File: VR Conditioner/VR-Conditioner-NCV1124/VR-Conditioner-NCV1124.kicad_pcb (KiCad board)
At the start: 2 copper layers, 18.7 x 17.9 mm, 9 parts, among them J1 NCV1124DR2G, J2 Board Conn

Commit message: Add prod files for NVC1124
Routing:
- added copper zone on B.Cu, net GND
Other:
- board text added: "Designed by Henrik Heininen HEINISET.FI (c) 2026"
- board text removed: "Designed by HEINISET.FI (c) 2026"
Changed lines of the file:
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@@
 			(usegerberattributes yes)
 			(usegerberadvancedattributes yes)
-			(creategerberjobfile yes)
+			(creategerberjobfile no)
 			(dashed_line_dash_ratio 12.000000)
 			(dashed_line_gap_ratio 3.000000)
@@
 			(outputformat 1)
 			(mirror no)
-			(drillshape 1)
+			(drillshape 0)
 			(scaleselection 1)
-			(outputdirectory "")
+			(outputdirectory "./gerbers")
 		)
 	)
@@
 			)
 		)
+		(property "LCSC" "C17414"
+			(at 0 0 0)
+			(layer "F.SilkS")
+			(hide yes)
+			(effects
+				(font
+					(size 1.27 1.27)
+					(thickness 0.15)
+				)
+			)
+		)
 		(property ki_fp_filters "R_*")
 		(sheetname "/")
@@
 			)
 		)
+		(property "LCSC" "C49678"
+			(at 0 0 0)
+			(layer "F.SilkS")
+			(hide yes)
+			(effects
+				(font
+					(size 1.27 1.27)
+					(thickness 0.15)
+				)
+			)
+		)
 		(property ki_fp_filters "C_*")
 		(sheetname "/")
@@
 			(at 0 0 90)
 			(layer "F.Fab")
+			(hide yes)
+			(effects
+				(font
+					(size 1.27 1.27)
+					(thickness 0.15)
+				)
+			)
+		)
+		(property "LCSC" "C17414"
+			(at 0 0 0)
+			(layer "F.SilkS")
 			(hide yes)
 			(effects
@@
 			)
 		)
+		(property "LCSC" "C49678"
+			(at 0 0 0)
+			(layer "F.SilkS")
+			(hide yes)
+			(effects
+				(font
+					(size 1.27 1.27)
+					(thickness 0.15)
+				)
+			)
+		)
 		(property ki_fp_filters "C_*")
 		(sheetname "/")
@@
 			)
 		)
+		(property "LCSC" "C49678"
+			(at 0 0 0)
+			(layer "F.SilkS")
+			(hide yes)
+			(effects
+				(font
+					(size 1.27 1.27)
+					(thickness 0.15)
+				)
+			)
+		)
 		(property ki_fp_filters "C_*")
 		(sheetname "/")
@@
 		(sheetname "/")
 		(sheetfile "VR-Conditioner-NCV1124.kicad_sch")
-		(attr smd)
+		(attr smd exclude_from_pos_files exclude_from_bom)
 		(fp_line
 			(start -0.261252 0.735)
@@
 				(font
 					(size 1 1)
+					(thickness 0.15)
+				)
+			)
+		)
+		(property "LCSC" "C152274"
+			(at 0 0 0)
+			(layer "F.SilkS")
+			(hide yes)
+			(effects
+				(font
+					(size 1.27 1.27)
 					(thickness 0.15)
 				)
@@
 		(layer "Edge.Cuts")
 	)
-	(gr_text "Designed by HEINISET.FI\n(c) 2026"
-		(at 155.194 77.216 0)
+	(gr_text "Designed by Henrik Heininen\nHEINISET.FI\n(c) 2026"
+		(at 155.2448 78.5368 0)
 		(layer "B.SilkS")
 		(effects
@@
 		(net 10)
 		(net_name "GND")
-		(layer "F.Cu")
+		(layers "F.Cu" "B.Cu")
 		(hatch edge 0.5)
 		(connect_pads yes

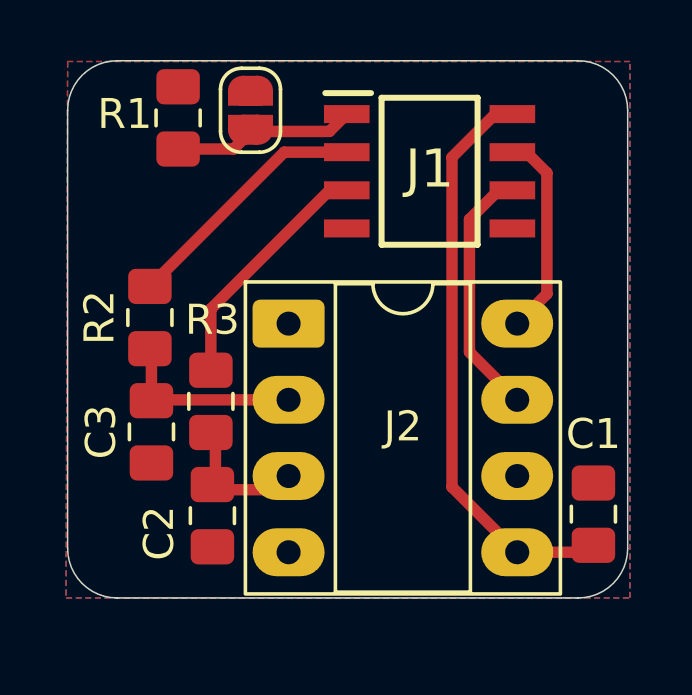
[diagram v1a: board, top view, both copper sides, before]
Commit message: Changed to THT resistors due to wattage requirements as per ncv1124 datasheet. Added prod files
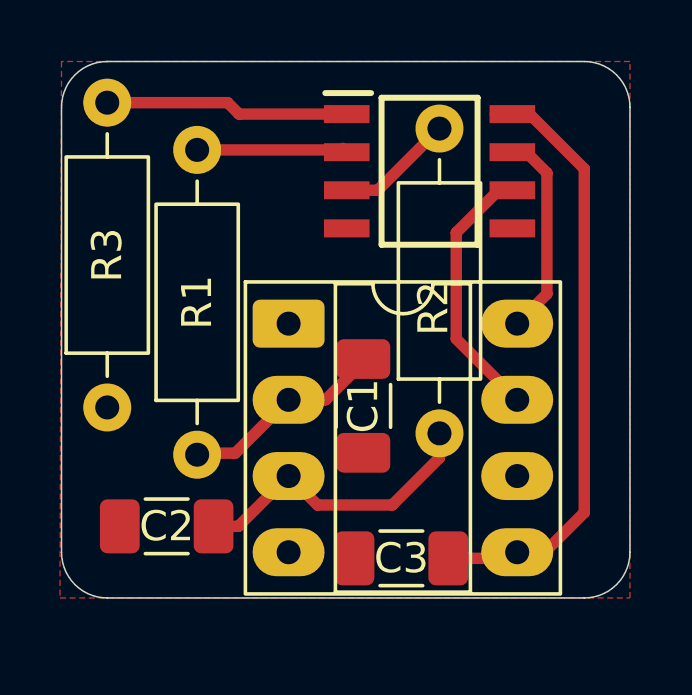
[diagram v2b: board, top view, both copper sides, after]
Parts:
- removed JP1: SolderJumper_2_Open, Jumper:SolderJumper-2_P1.3mm_Open_RoundedPad1.0x1.5mm
- C1: renamed from C3; value 100n -> 1nF; footprint Capacitor_SMD:C_0805_2012Metric_Pad1.18x1.45mm_HandSolder -> Capacitor_SMD:C_1206_3216Metric_Pad1.33x1.80mm_HandSolder
- C2: value 100n -> 1nF; footprint Capacitor_SMD:C_0805_2012Metric_Pad1.18x1.45mm_HandSolder -> Capacitor_SMD:C_1206_3216Metric_Pad1.33x1.80mm_HandSolder
- C3: renamed from C1; footprint Capacitor_SMD:C_0805_2012Metric_Pad1.18x1.45mm_HandSolder -> Capacitor_SMD:C_1206_3216Metric_Pad1.33x1.80mm_HandSolder
- R1: renamed from R2; value 10k -> 15k; footprint Capacitor_SMD:C_0805_2012Metric_Pad1.18x1.45mm_HandSolder -> Resistor_THT:R_Axial_DIN0207_L6.3mm_D2.5mm_P10.16mm_Horizontal
- R2: renamed from R3; value 10k -> 15k; footprint Capacitor_SMD:C_0805_2012Metric_Pad1.18x1.45mm_HandSolder -> Resistor_THT:R_Axial_DIN0207_L6.3mm_D2.5mm_P10.16mm_Horizontal
- R3: renamed from R1; value Rtrip -> Rtrip / 17k8; footprint Capacitor_SMD:C_0805_2012Metric_Pad1.18x1.45mm_HandSolder -> Resistor_THT:R_Axial_DIN0207_L6.3mm_D2.5mm_P10.16mm_Horizontal
- moved R3 9.94 mm to (147.1, 86.6), turned to 90 degrees
- moved R2 7.69 mm to (158.2, 87.5)
- moved C1 7.11 mm to (155.7, 86.6)
- moved C3 6.57 mm to (156.9, 91.6), turned to 0 degrees
- moved R1 4.84 mm to (150.1, 88.2)
- moved C2 1.56 mm to (149.1, 90.6), turned to 180 degrees
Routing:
- net IN2+: track 4.60 -> 10.1 mm
- net Net-(J1-IN2): track 8.21 -> 4.52 mm
- net Net-(J1-IN1): track 8.42 -> 5.20 mm
- net Net-(J1-INADJ): track 6.10 -> 8.14 mm
- net IN1+: track 6.23 -> 7.43 mm
- net VCC: track 19.3 -> 20.4 mm
- removed copper zone on B.Cu, net GND
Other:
- board size 18.7 x 17.9 mm -> 18.9 x 17.9 mm

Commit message: Small brainfart with the layout. Updated pcb and gerbers
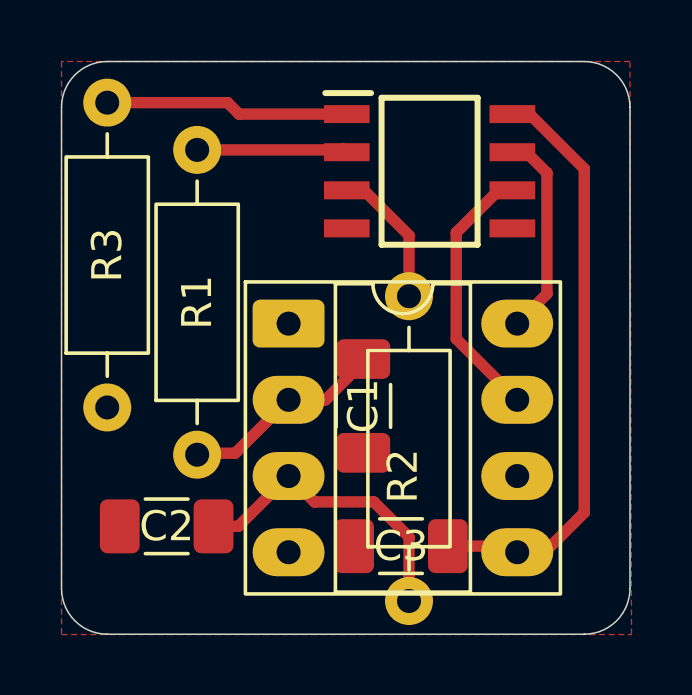
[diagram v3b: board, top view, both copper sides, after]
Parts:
- moved R2 5.68 mm to (157.2, 93.1)
- moved C3 0.41 mm to (156.9, 91.2)
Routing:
- net Net-(J1-IN2): track 4.52 -> 5.30 mm
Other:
- board size 18.9 x 17.9 mm -> 18.9 x 19.1 mm
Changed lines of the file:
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@@
 	(footprint "Capacitor_SMD:C_1206_3216Metric_Pad1.33x1.80mm_HandSolder"
 		(layer "F.Cu")
-		(at 156.9212 91.6432)
+		(at 156.9089 91.2368)
 		(descr "Capacitor SMD 1206 (3216 Metric), square (rectangular) end terminal, IPC-7351 nominal with elongated pad for handsoldering. (Body size source: IPC-SM-782 page 76, https://www.pcb-3d.com/wordpress/wp-content/uploads/ipc-sm-782a_amendment_1_and_2.pdf), generated with kicad-footprint-generator")
 		(tags "capacitor handsolder")
@@
 	(footprint "Resistor_THT:R_Axial_DIN0207_L6.3mm_D2.5mm_P10.16mm_Horizontal"
 		(layer "F.Cu")
-		(at 158.1912 87.4776 90)
+		(at 157.1752 93.0656 90)
 		(descr "Resistor, Axial_DIN0207 series, Axial, Horizontal, pin pitch=10.16mm, 0.25W = 1/4W, length*diameter=6.3*2.5mm^2, http://cdn-reichelt.de/documents/datenblatt/B400/1_4W%23YAG.pdf")
 		(tags "Resistor Axial_DIN0207 series Axial Horizontal pin pitch 10.16mm 0.25W = 1/4W length 6.3mm diameter 2.5mm")
@@
 	)
 	(gr_arc
-		(start 147.1168 92.964)
-		(mid 146.039169 92.517631)
-		(end 145.5928 91.44)
+		(start 147.1168 94.172369)
+		(mid 146.039169 93.726)
+		(end 145.5928 92.648369)
 		(stroke
 			(width 0.05)
@@
 	)
 	(gr_line
-		(start 164.5412 91.44)
+		(start 164.5412 92.6484)
 		(end 164.5412 76.6064)
 		(stroke
@@
 	)
 	(gr_arc
-		(start 164.5412 91.44)
-		(mid 164.094831 92.517631)
-		(end 163.0172 92.964)
+		(start 164.5412 92.648369)
+		(mid 164.094831 93.726)
+		(end 163.0172 94.172369)
 		(stroke
 			(width 0.05)
@@
 	(gr_line
 		(start 145.5928 76.6064)
-		(end 145.5928 91.44)
+		(end 145.5928 92.648369)
 		(stroke
 			(width 0.05)
@@
 	)
 	(gr_line
-		(start 147.1168 92.964)
-		(end 163.0172 92.964)
+		(start 147.1168 94.172369)
+		(end 163.0172 94.172369)
 		(stroke
 			(width 0.05)
@@
 	)
 	(segment
+		(start 158.4714 91.2368)
+		(end 160.5788 91.2368)
+		(width 0.381)
+		(layer "F.Cu")
+		(net 1)
+	)
+	(segment
 		(start 163.0172 90.1192)
 		(end 163.0172 78.6582)
@@
 	)
 	(segment
-		(start 158.4837 91.6432)
-		(end 160.5788 91.6432)
+		(start 160.5788 91.2368)
+		(end 160.782 91.44)
 		(width 0.381)
 		(layer "F.Cu")
@@
 	)
 	(segment
-		(start 154.1272 89.8652)
-		(end 153.162 88.9)
+		(start 157.1752 90.932)
+		(end 157.1752 93.0656)
+		(width 0.381)
+		(layer "F.Cu")
+		(net 2)
+	)
+	(segment
+		(start 156.0068 89.7636)
+		(end 157.1752 90.932)
+		(width 0.381)
+		(layer "F.Cu")
+		(net 2)
+	)
+	(segment
+		(start 154.0256 89.7636)
+		(end 156.0068 89.7636)
+		(width 0.381)
+		(layer "F.Cu")
+		(net 2)
+	)
+	(segment
+		(start 153.162 88.9)
+		(end 154.0256 89.7636)
 		(width 0.381)
 		(layer "F.Cu")
@@
 	)
 	(segment
-		(start 156.6164 89.8652)
-		(end 154.1272 89.8652)
-		(width 0.381)
-		(layer "F.Cu")
-		(net 2)
-	)
-	(segment
-		(start 158.1912 88.2904)
-		(end 156.6164 89.8652)
-		(width 0.381)
-		(layer "F.Cu")
-		(net 2)
-	)
-	(segment
 		(start 153.162 88.9)
 		(end 151.4856 90.5764)
@@
 	)
 	(segment
-		(start 158.1912 87.4776)
-		(end 158.1912 88.2904)
-		(width 0.381)
-		(layer "F.Cu")
-		(net 2)
-	)
-	(segment
 		(start 149.733 88.138)
 		(end 151.384 88.138)
@@
 	)
 	(segment
+		(start 155.101 79.375)
+		(end 155.674 79.375)
+		(width 0.381)
+		(layer "F.Cu")
+		(net 4)
+	)
+	(segment
 		(start 154.528 79.375)
 		(end 155.101 79.375)
@@
 	)
 	(segment
-		(start 155.101 79.375)
-		(end 156.1338 79.375)
+		(start 155.674 79.375)
+		(end 157.1752 80.8762)
 		(width 0.381)
 		(layer "F.Cu")
@@
 	)
 	(segment
-		(start 156.1338 79.375)
-		(end 158.1912 77.3176)
+		(start 157.1752 80.8762)
+		(end 157.1752 82.9056)
 		(width 0.381)
 		(layer "F.Cu")
@@
 		(hatch edge 0.5)
 		(connect_pads yes
-			(clearance 0.5)
+			(clearance 0.3)
 		)
 		(min_thickness 0.25)
@@
 		(polygon
 			(pts
-				(xy 145.5928 75.0824) (xy 145.542 92.964) (xy 164.5412 92.964) (xy 164.5412 75.0824)
-			)
-		)
+				(xy 145.5928 75.0824) (xy 145.5928 94.1832) (xy 164.592 94.1832) (xy 164.5412 75.0824)
+			)
+		)
